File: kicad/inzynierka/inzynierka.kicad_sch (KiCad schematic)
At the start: 17 parts

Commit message: Dodanie pozycji mikrofonów B
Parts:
- added MICB1, MICB10, MICB11, MICB12, MICB13, MICB14, MICB15, MICB16, MICB17, MICB18, MICB19, MICB2, MICB20, MICB3, MICB4, MICB5, MICB6, MICB7, MICB8, MICB9: ~, _moje:INMP441 breakout, symbol _Moje:INMP441
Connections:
- net +3.3V: now also MICB1.1 (L/R), MICB1.5 (VDD), MICB10.1 (L/R), MICB10.5 (VDD), MICB11.1 (L/R), MICB11.5 (VDD), MICB12.1 (L/R), MICB12.5 (VDD), MICB13.1 (L/R), MICB13.5 (VDD), MICB14.1 (L/R), MICB14.5 (VDD), MICB15.1 (L/R), MICB15.5 (VDD), MICB16.1 (L/R), MICB16.5 (VDD), MICB17.1 (L/R), MICB17.5 (VDD), MICB18.1 (L/R), MICB18.5 (VDD), MICB19.1 (L/R), MICB19.5 (VDD), MICB2.1 (L/R), MICB2.5 (VDD), MICB20.1 (L/R), MICB20.5 (VDD), MICB3.1 (L/R), MICB3.5 (VDD), MICB4.1 (L/R), MICB4.5 (VDD), MICB5.1 (L/R), MICB5.5 (VDD), MICB6.1 (L/R), MICB6.5 (VDD), MICB7.1 (L/R), MICB7.5 (VDD), MICB8.1 (L/R), MICB8.5 (VDD), MICB9.1 (L/R), MICB9.5 (VDD)
- net CLK1: now also MICB1.3 (CLK), MICB10.3 (CLK), MICB11.3 (CLK), MICB12.3 (CLK), MICB13.3 (CLK), MICB14.3 (CLK), MICB15.3 (CLK), MICB16.3 (CLK), MICB17.3 (CLK), MICB18.3 (CLK), MICB19.3 (CLK), MICB2.3 (CLK), MICB20.3 (CLK), MICB3.3 (CLK), MICB4.3 (CLK), MICB5.3 (CLK), MICB6.3 (CLK), MICB7.3 (CLK), MICB8.3 (CLK), MICB9.3 (CLK)
- net CLK2: now also MICB1.2 (WS), MICB10.2 (WS), MICB11.2 (WS), MICB12.2 (WS), MICB13.2 (WS), MICB14.2 (WS), MICB15.2 (WS), MICB16.2 (WS), MICB17.2 (WS), MICB18.2 (WS), MICB19.2 (WS), MICB2.2 (WS), MICB20.2 (WS), MICB3.2 (WS), MICB4.2 (WS), MICB5.2 (WS), MICB6.2 (WS), MICB7.2 (WS), MICB8.2 (WS), MICB9.2 (WS)
- net D1: now also MICB1.6 (SD)
- net D10: now also MICB10.6 (SD)
- net D11: now also MICB11.6 (SD)
- net D12: now also MICB12.6 (SD)
- net D13: now also MICB13.6 (SD)
- net D14: now also MICB14.6 (SD)
- net D15: now also MICB15.6 (SD)
- net D16: now also MICB16.6 (SD)
- net D17: now also MICB17.6 (SD)
- net D18: now also MICB18.6 (SD)
- net D19: now also MICB19.6 (SD)
- net D2: now also MICB2.6 (SD)
- net D20: now also MICB20.6 (SD)
- net D3: now also MICB3.6 (SD)
- net D4: now also MICB4.6 (SD)
- net D5: now also MICB5.6 (SD)
- net D6: now also MICB6.6 (SD)
- net D7: now also MICB7.6 (SD)
- net D8: now also MICB8.6 (SD)
- net D9: now also MICB9.6 (SD)
- net GND: now also MICB1.4 (GND), MICB10.4 (GND), MICB11.4 (GND), MICB12.4 (GND), MICB13.4 (GND), MICB14.4 (GND), MICB15.4 (GND), MICB16.4 (GND), MICB17.4 (GND), MICB18.4 (GND), MICB19.4 (GND), MICB2.4 (GND), MICB20.4 (GND), MICB3.4 (GND), MICB4.4 (GND), MICB5.4 (GND), MICB6.4 (GND), MICB7.4 (GND), MICB8.4 (GND), MICB9.4 (GND)
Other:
- moved on the sheet: MICA1, MICA10, MICA11, MICA12, MICA13, MICA14, MICA15, MICA16, MICA2, MICA3, MICA4, MICA5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

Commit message: Dodanie biblioteki footprintów do projektu
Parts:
- MICA1, MICA10, MICA11, MICA12, MICA13, MICA14, MICA15, MICA16, MICA2, MICA3, MICA4, MICA5, MICA6, MICA7, MICA8, MICA9, MICB1, MICB10, MICB11, MICB12, MICB13, MICB14, MICB15, MICB16, MICB17, MICB18, MICB19, MICB2, MICB20, MICB3, MICB4, MICB5, MICB6, MICB7, MICB8, MICB9: footprint _moje:INMP441 breakout -> Moje:INMP441 breakout
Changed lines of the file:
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@@
 			)
 		)
-		(property "Footprint" "_moje:INMP441 breakout"
+		(property "Footprint" "Moje:INMP441 breakout"
 			(at 77.47 134.62 0)
 			(effects
@@
 			)
 		)
-		(property "Footprint" "_moje:INMP441 breakout"
+		(property "Footprint" "Moje:INMP441 breakout"
 			(at 152.4 35.56 0)
 			(effects
@@
 			)
 		)
-		(property "Footprint" "_moje:INMP441 breakout"
+		(property "Footprint" "Moje:INMP441 breakout"
 			(at 40.64 78.74 0)
 			(effects
@@
 			)
 		)
-		(property "Footprint" "_moje:INMP441 breakout"
+		(property "Footprint" "Moje:INMP441 breakout"
 			(at 77.47 148.59 0)
 			(effects
@@
 			)
 		)
-		(property "Footprint" "_moje:INMP441 breakout"
+		(property "Footprint" "Moje:INMP441 breakout"
 			(at 77.47 49.53 0)
 			(effects
@@
 			)
 		)
-		(property "Footprint" "_moje:INMP441 breakout"
+		(property "Footprint" "Moje:INMP441 breakout"
 			(at 115.57 49.53 0)
 			(effects
@@
 			)
 		)
-		(property "Footprint" "_moje:INMP441 breakout"
+		(property "Footprint" "Moje:INMP441 breakout"
 			(at 115.57 63.5 0)
 			(effects
@@
 			)
 		)
-		(property "Footprint" "_moje:INMP441 breakout"
+		(property "Footprint" "Moje:INMP441 breakout"
 			(at 152.4 63.5 0)
 			(effects
@@
 			)
 		)
-		(property "Footprint" "_moje:INMP441 breakout"
+		(property "Footprint" "Moje:INMP441 breakout"
 			(at 115.57 21.59 0)
 			(effects
@@
 			)
 		)
-		(property "Footprint" "_moje:INMP441 breakout"
+		(property "Footprint" "Moje:INMP441 breakout"
 			(at 115.57 77.47 0)
 			(effects
@@
 			)
 		)
-		(property "Footprint" "_moje:INMP441 breakout"
+		(property "Footprint" "Moje:INMP441 breakout"
 			(at 77.47 92.71 0)
 			(effects
@@
 			)
 		)
-		(property "Footprint" "_moje:INMP441 breakout"
+		(property "Footprint" "Moje:INMP441 breakout"
 			(at 77.47 120.65 0)
 			(effects
@@
 			)
 		)
-		(property "Footprint" "_moje:INMP441 breakout"
+		(property "Footprint" "Moje:INMP441 breakout"
 			(at 152.4 105.41 0)
 			(effects
@@
 			)
 		)
-		(property "Footprint" "_moje:INMP441 breakout"
+		(property "Footprint" "Moje:INMP441 breakout"
 			(at 152.4 91.44 0)
 			(effects
@@
 			)
 		)
-		(property "Footprint" "_moje:INMP441 breakout"
+		(property "Footprint" "Moje:INMP441 breakout"
 			(at 152.4 77.47 0)
 			(effects
@@
 			)
 		)
-		(property "Footprint" "_moje:INMP441 breakout"
+		(property "Footprint" "Moje:INMP441 breakout"
 			(at 152.4 21.59 0)
 			(effects
@@
 			)
 		)
-		(property "Footprint" "_moje:INMP441 breakout"
+		(property "Footprint" "Moje:INMP441 breakout"
 			(at 77.47 106.68 0)
 			(effects
@@
 			)
 		)
-		(property "Footprint" "_moje:INMP441 breakout"
+		(property "Footprint" "Moje:INMP441 breakout"
 			(at 77.47 78.74 0)
 			(effects
@@
 			)
 		)
-		(property "Footprint" "_moje:INMP441 breakout"
+		(property "Footprint" "Moje:INMP441 breakout"
 			(at 152.4 49.53 0)
 			(effects
@@
 			)
 		)
-		(property "Footprint" "_moje:INMP441 breakout"
+		(property "Footprint" "Moje:INMP441 breakout"
 			(at 40.64 120.65 0)
 			(effects
@@
 			)
 		)
-		(property "Footprint" "_moje:INMP441 breakout"
+		(property "Footprint" "Moje:INMP441 breakout"
 			(at 115.57 35.56 0)
 			(effects
@@
 			)
 		)
-		(property "Footprint" "_moje:INMP441 breakout"
+		(property "Footprint" "Moje:INMP441 breakout"
 			(at 40.64 92.71 0)
 			(effects
@@
 			)
 		)
-		(property "Footprint" "_moje:INMP441 breakout"
+		(property "Footprint" "Moje:INMP441 breakout"
 			(at 40.64 134.62 0)
 			(effects
@@
 			)
 		)
-		(property "Footprint" "_moje:INMP441 breakout"
+		(property "Footprint" "Moje:INMP441 breakout"
 			(at 115.57 91.44 0)
 			(effects
@@
 			)
 		)
-		(property "Footprint" "_moje:INMP441 breakout"
+		(property "Footprint" "Moje:INMP441 breakout"
 			(at 40.64 63.5 0)
 			(effects
@@
 			)
 		)
-		(property "Footprint" "_moje:INMP441 breakout"
+		(property "Footprint" "Moje:INMP441 breakout"
 			(at 40.64 106.68 0)
 			(effects
@@
 			)
 		)
-		(property "Footprint" "_moje:INMP441 breakout"
+		(property "Footprint" "Moje:INMP441 breakout"
 			(at 40.64 49.53 0)
 			(effects
@@
 			)
 		)
-		(property "Footprint" "_moje:INMP441 breakout"
+		(property "Footprint" "Moje:INMP441 breakout"
 			(at 77.47 21.59 0)
 			(effects
@@
 			)
 		)
-		(property "Footprint" "_moje:INMP441 breakout"
+		(property "Footprint" "Moje:INMP441 breakout"
 			(at 77.47 35.56 0)
 			(effects
@@
 			)
 		)
-		(property "Footprint" "_moje:INMP441 breakout"
+		(property "Footprint" "Moje:INMP441 breakout"
 			(at 40.64 21.59 0)
 			(effects
@@
 			)
 		)
-		(property "Footprint" "_moje:INMP441 breakout"
+		(property "Footprint" "Moje:INMP441 breakout"
 			(at 115.57 105.41 0)
 			(effects
@@
 			)
 		)
-		(property "Footprint" "_moje:INMP441 breakout"
+		(property "Footprint" "Moje:INMP441 breakout"
 			(at 115.57 119.38 0)
 			(effects
@@
 			)
 		)
-		(property "Footprint" "_moje:INMP441 breakout"
+		(property "Footprint" "Moje:INMP441 breakout"
 			(at 40.64 35.56 0)
 			(effects
@@
 			)
 		)
-		(property "Footprint" "_moje:INMP441 breakout"
+		(property "Footprint" "Moje:INMP441 breakout"
 			(at 152.4 119.38 0)
 			(effects
@@
 			)
 		)
-		(property "Footprint" "_moje:INMP441 breakout"
+		(property "Footprint" "Moje:INMP441 breakout"
 			(at 40.64 148.59 0)
 			(effects
@@
 			)
 		)
-		(property "Footprint" "_moje:INMP441 breakout"
+		(property "Footprint" "Moje:INMP441 breakout"
 			(at 77.47 63.5 0)
 			(effects

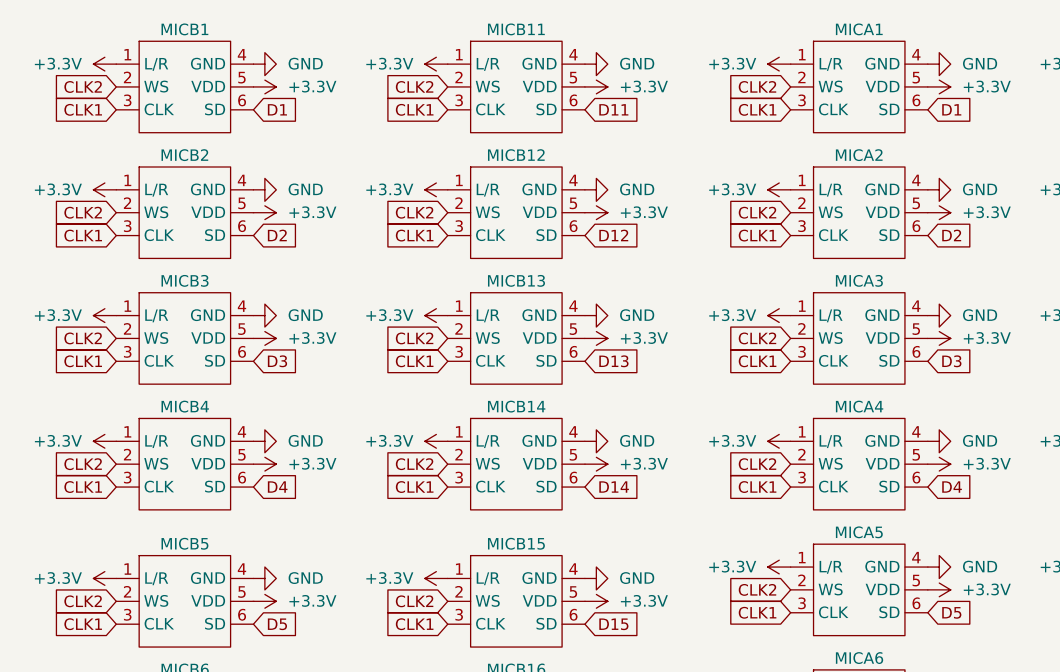
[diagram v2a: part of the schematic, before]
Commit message: Dodanie innego ustawienia głośników na płytkę
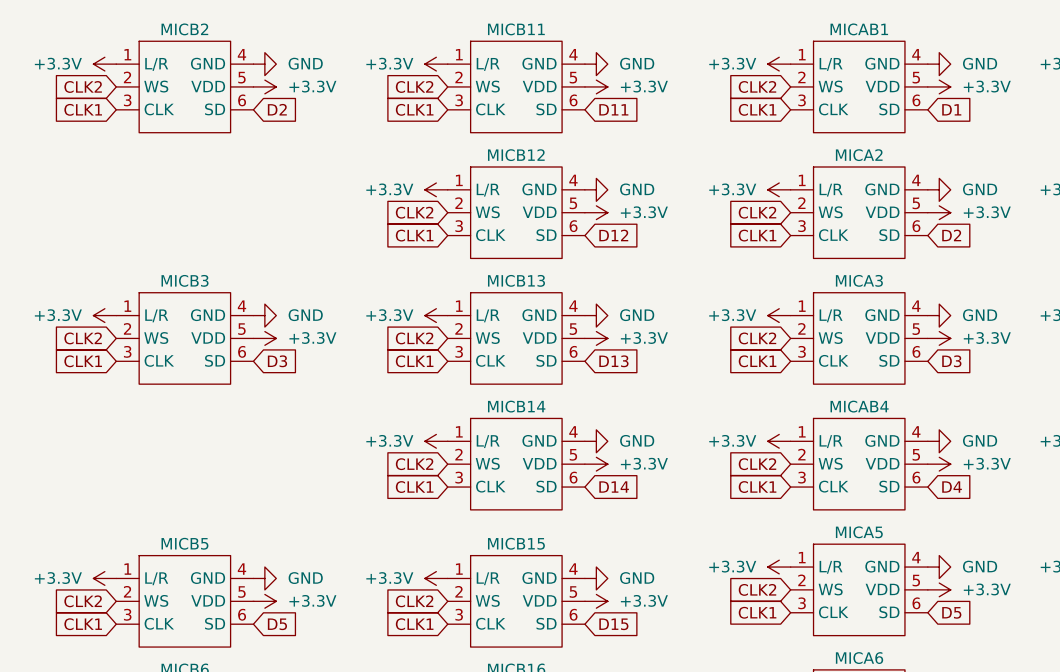
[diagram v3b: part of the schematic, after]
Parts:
- removed MICB2, MICB4: ~, Moje:INMP441 breakout, symbol _Moje:INMP441
- renumbered MICA1 to MICAB1, MICA4 to MICAB4, MICB1 to MICB2
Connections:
- net D1: no longer MICB2.6 (SD)
- net D2: now also MICB2.6 (SD)

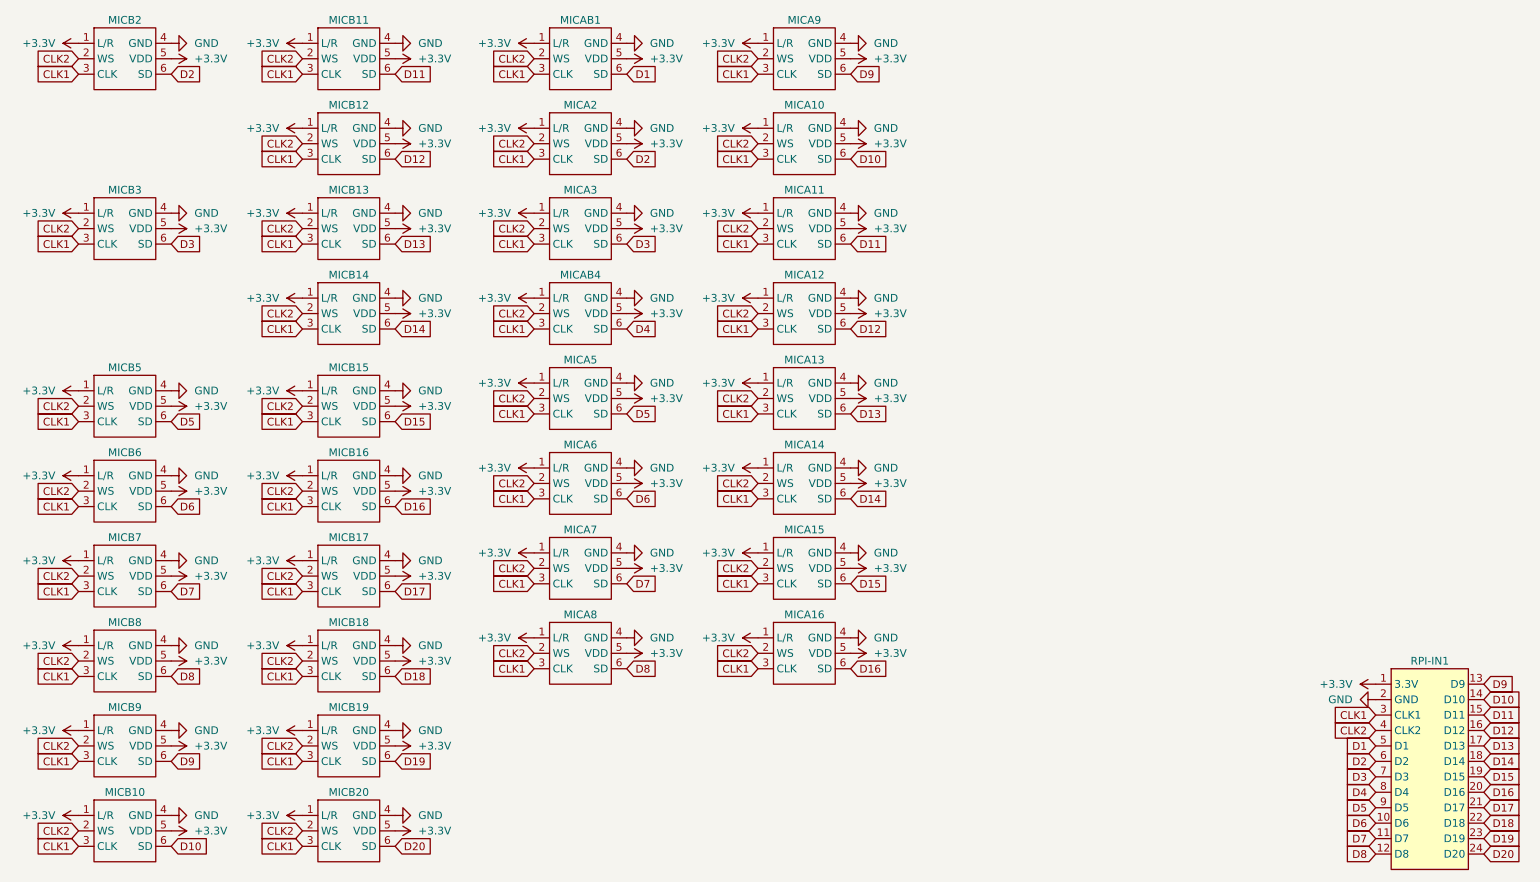
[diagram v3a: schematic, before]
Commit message: Dodanie opisów do footprintów
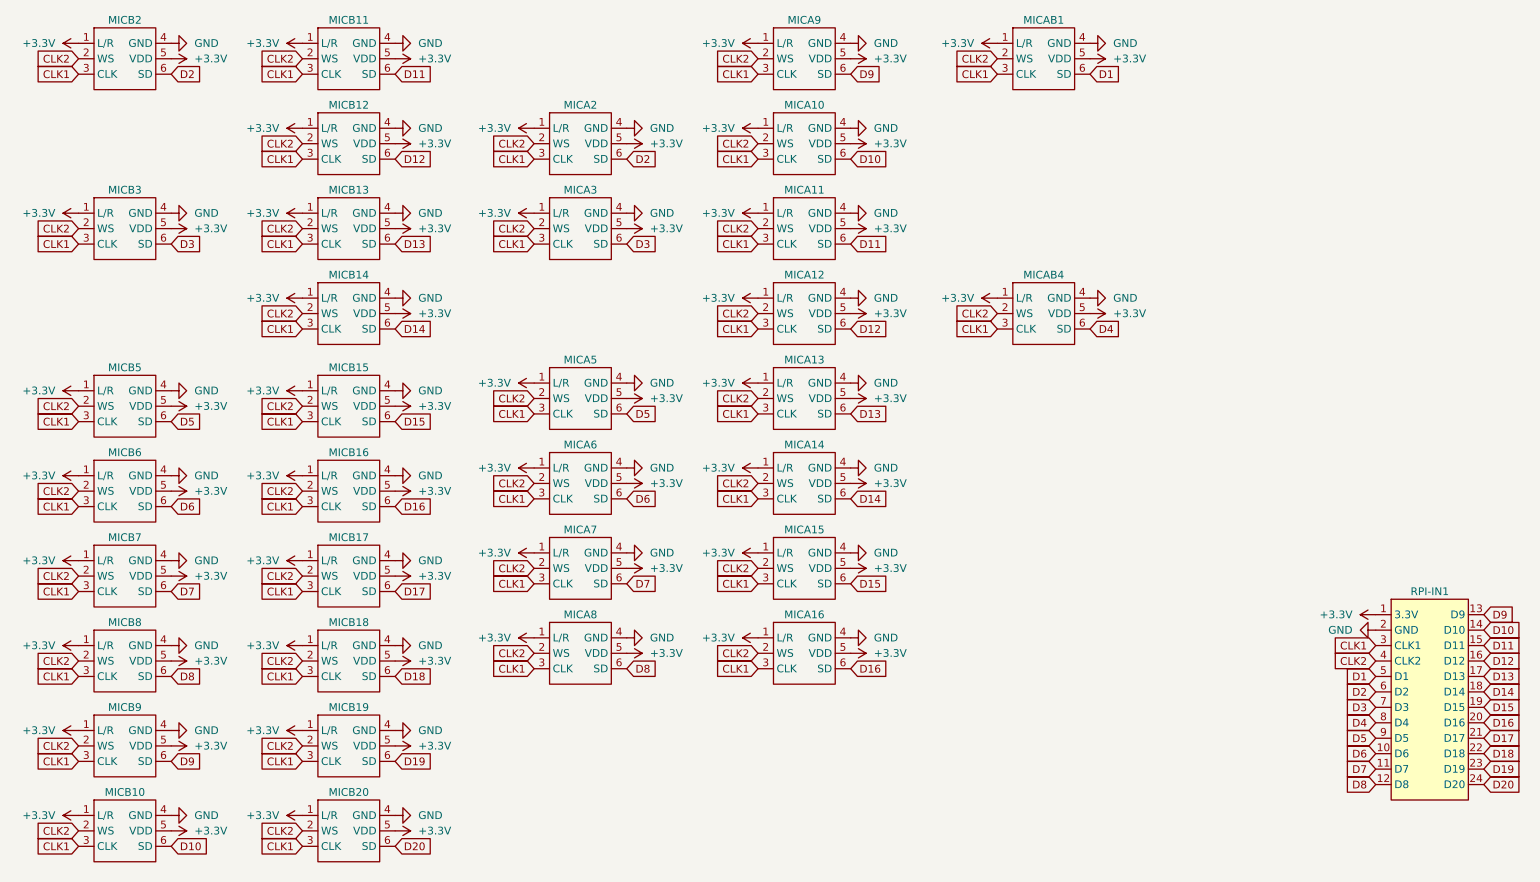
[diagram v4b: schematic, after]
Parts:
- RPI-IN1: footprint Connector_PinSocket_2.54mm:PinSocket_2x10_P2.54mm_Vertical -> Moje:RPI-IN1
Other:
- moved on the sheet: MICAB1, MICAB4, RPI-IN1

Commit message: Podłączenie L/R na głośnikach do GND
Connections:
- net +3.3V: no longer MICA10.1 (L/R), MICA11.1 (L/R), MICA12.1 (L/R), MICA13.1 (L/R), MICA14.1 (L/R), MICA15.1 (L/R), MICA16.1 (L/R), MICA2.1 (L/R), MICA3.1 (L/R), MICA5.1 (L/R), MICA6.1 (L/R), MICA7.1 (L/R), MICA8.1 (L/R), MICA9.1 (L/R), MICAB1.1 (L/R), MICAB4.1 (L/R), MICB10.1 (L/R), MICB11.1 (L/R), MICB12.1 (L/R), MICB13.1 (L/R), MICB14.1 (L/R), MICB15.1 (L/R), MICB16.1 (L/R), MICB17.1 (L/R), MICB18.1 (L/R), MICB19.1 (L/R), MICB2.1 (L/R), MICB20.1 (L/R), MICB3.1 (L/R), MICB5.1 (L/R), MICB6.1 (L/R), MICB7.1 (L/R), MICB8.1 (L/R), MICB9.1 (L/R)
- net GND: now also MICA10.1 (L/R), MICA11.1 (L/R), MICA12.1 (L/R), MICA13.1 (L/R), MICA14.1 (L/R), MICA15.1 (L/R), MICA16.1 (L/R), MICA2.1 (L/R), MICA3.1 (L/R), MICA5.1 (L/R), MICA6.1 (L/R), MICA7.1 (L/R), MICA8.1 (L/R), MICA9.1 (L/R), MICAB1.1 (L/R), MICAB4.1 (L/R), MICB10.1 (L/R), MICB11.1 (L/R), MICB12.1 (L/R), MICB13.1 (L/R), MICB14.1 (L/R), MICB15.1 (L/R), MICB16.1 (L/R), MICB17.1 (L/R), MICB18.1 (L/R), MICB19.1 (L/R), MICB2.1 (L/R), MICB20.1 (L/R), MICB3.1 (L/R), MICB5.1 (L/R), MICB6.1 (L/R), MICB7.1 (L/R), MICB8.1 (L/R), MICB9.1 (L/R)

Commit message: Dokończenie trasowania 3.3V
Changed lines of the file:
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@@
 	(generator_version "9.0")
 	(paper "A4")
+	(wire
+		(pts
+			(xy 241.3 119.38) (xy 247.65 119.38)
+		)
+		(stroke
+			(width 0)
+			(type default)
+		)
+	)
 	(global_label "D12"
 		(shape input)
@@
 		)
 	)
+	(netclass_flag ""
+		(length 2.54)
+		(shape round)
+		(at 242.57 119.38 0)
+		(fields_autoplaced yes)
+		(effects
+			(font
+				(size 1.27 1.27)
+			)
+			(justify left bottom)
+		)
+		(property "Netclass" "3.3V"
+			(at 243.2685 116.84 0)
+			(effects
+				(font
+					(size 1.27 1.27)
+				)
+				(justify left)
+			)
+		)
+		(property "Component Class" ""
+			(at -44.45 2.54 0)
+			(effects
+				(font
+					(size 1.27 1.27)
+					(italic yes)
+				)
+			)
+		)
+	)
 	(symbol
 		(lib_id "_Moje:INMP441")
@@
 	(symbol
 		(lib_id "power:+3.3V")
-		(at 247.65 119.38 90)
+		(at 241.3 119.38 90)
 		(unit 1)
 		(exclude_from_sim no)
@@
 		(fields_autoplaced yes)
 		(property "Reference" "#PWR04"
-			(at 251.46 119.38 0)
+			(at 245.11 119.38 0)
 			(effects
 				(font
@@
 		)
 		(property "Value" "+3.3V"
-			(at 243.84 119.3799 90)
+			(at 237.49 119.3799 90)
 			(effects
 				(font
@@
 		)
 		(property "Footprint" ""
-			(at 247.65 119.38 0)
+			(at 241.3 119.38 0)
 			(effects
 				(font
@@
 		)
 		(property "Datasheet" ""
-			(at 247.65 119.38 0)
+			(at 241.3 119.38 0)
 			(effects
 				(font
@@
 		)
 		(property "Description" "Power symbol creates a global label with name \"+3.3V\""
-			(at 247.65 119.38 0)
+			(at 241.3 119.38 0)
 			(effects
 				(font

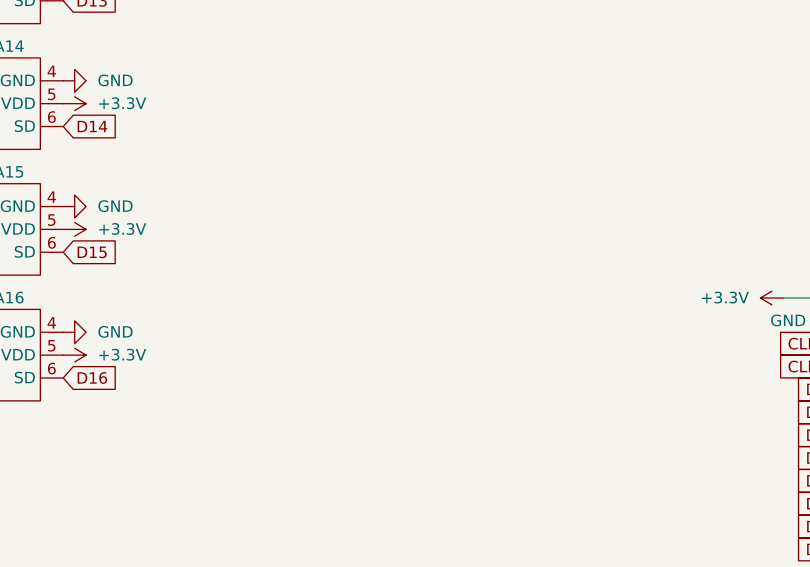
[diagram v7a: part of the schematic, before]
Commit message: Dodanie padów testowych
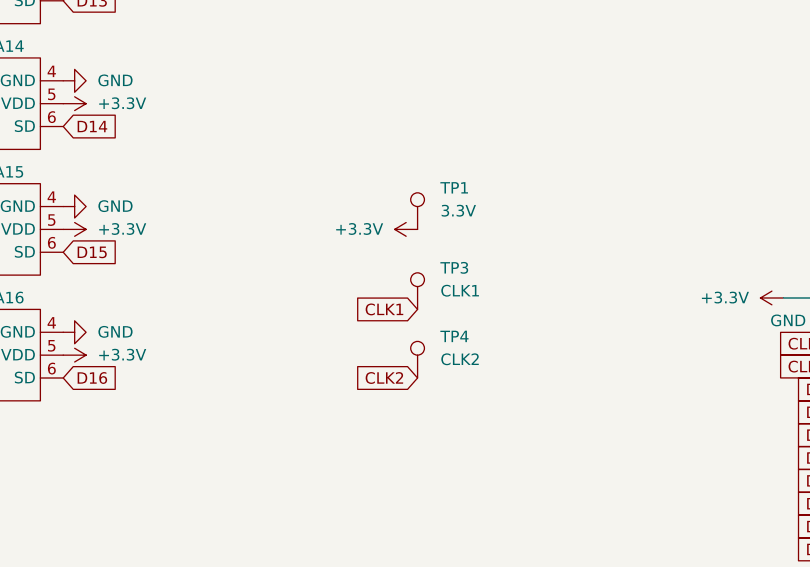
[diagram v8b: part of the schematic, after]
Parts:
- added TP1: 3.3V, symbol Connector:TestPoint
- added TP3: CLK1, symbol Connector:TestPoint
- added TP4: CLK2, symbol Connector:TestPoint
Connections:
- net +3.3V: now also TP1.1
- net CLK1: now also TP3.1
- net CLK2: now also TP4.1
